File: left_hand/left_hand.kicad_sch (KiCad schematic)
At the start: 44 parts, among them J1 8P8C_Shielded, J2 Conn_01x03, J3 Conn_01x08, J4 Conn_01x08, M1 Motor_Servo, M2 Motor_Servo, M3 Motor_Servo, M4 Motor_Servo, M5 Motor_Servo, Q1 Q_NMOS_GDS, Q2 Q_NMOS_GDS, Q3 Q_NMOS_GDS, Q4 Q_NMOS_GDS, Q5 Q_NMOS_GDS, U1 MCP23017_SP, U2 PCA9615DP, U3 PCA9685PW

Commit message: Major update
Hand PCB mostly complete
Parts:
- removed C3: 0.1uF, Capacitor_THT:C_Disc_D8.0mm_W2.5mm_P5.00mm, symbol Device:C
- removed J2: Conn_01x03, Connector_PinHeader_2.54mm:PinHeader_1x03_P2.54mm_Vertical, symbol Connector_Generic:Conn_01x03
- removed J3: Conn_01x08, Connector_PinHeader_2.54mm:PinHeader_1x08_P2.54mm_Vertical, symbol Connector_Generic:Conn_01x08
- removed R1, R3, R4, R6: 120R, symbol Device:R_US
- removed R2, R5: 600R, symbol Device:R_US
- removed R7, R8: 10kR, symbol Device:R_US
- removed SO1, SO2, SO3, SO4, SO5: ~, symbol bh_symbol_library:SOLENOID
- removed U2: PCA9615DP, Package_SO:TSSOP-10_3x3mm_P0.5mm, symbol Interface:PCA9615DP
- added D6, D7: LED, LED_THT:LED_D5.0mm_Clear, symbol Device:LED
- added H1, H2, H3, H4: MountingHole, MountingHole:MountingHole_3.2mm_M3, symbol Mechanical:MountingHole
- added J5: Conn_02x02_Top_Bottom, Connector_Molex:Molex_Mini-Fit_Jr_5569-04A2_2x02_P4.20mm_Horizontal, symbol Connector_Generic:Conn_02x02_Top_Bottom
- added J6: Screw_Terminal_01x10, TerminalBlock_Phoenix:TerminalBlock_Phoenix_PT-1,5-10-5.0-H_1x10_P5.00mm_Horizontal, symbol Connector:Screw_Terminal_01x10
- added R14, R15: 330R, Resistor_THT:R_Axial_DIN0207_L6.3mm_D2.5mm_P10.16mm_Horizontal, symbol Device:R_US
- C1, C2: footprint Capacitor_THT:C_Disc_D8.0mm_W2.5mm_P5.00mm -> Capacitor_THT:C_Disc_D3.4mm_W2.1mm_P2.50mm
- J1: footprint Connector_RJ:RJ45_Amphenol_RJHSE5380 -> Connector_RJ:RJ45_Amphenol_54602-x08_Horizontal; Digikey (none) -> https://www.digikey.ca/en/products/detail/amphenol-cs-fci/5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
- M1, M2, M3, M4, M5: footprint Connector_PinHeader_2.54mm:PinHeader_1x03_P2.54mm_Horizontal -> Connector_PinHeader_2.54mm:PinHeader_1x03_P2.54mm_Vertical
- R10, R11, R12, R13, R9: footprint (none) -> Resistor_THT:R_Axial_DIN0207_L6.3mm_D2.5mm_P10.16mm_Horizontal
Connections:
- net +12V: now also J5.3 (Pin_3), J6.10 (Pin_10), J6.2 (Pin_2), J6.4 (Pin_4), J6.6 (Pin_6), J6.8 (Pin_8); no longer J1.7
- net +5V: now also J5.4 (Pin_4); no longer J1.5
- net DSCL+: now also J1.4; no longer J1.2
- net DSCL-: now also J1.3; no longer J1.1
- net DSDA+: now also J1.5; no longer J1.4
- net DSDA-: now also J1.6; no longer J1.3
- net GND: now also J1.1, J1.2, J1.7, J5.1 (Pin_1), J5.2 (Pin_2), R14.2, R15.2; no longer J1.6
- net at D5.2 (A), Q5.2 (D): now also J6.1 (Pin_1)
- net LED1: now reaches U1.26 (GPA5)
- net LED1: now also D6.2 (A)
- net LED2: now reaches U1.27 (GPA6)
- net LED2: now also D7.2 (A)
- net at D2.2 (A), Q2.2 (D): now also J6.7 (Pin_7)
- net at D3.2 (A), Q3.2 (D): now also J6.5 (Pin_5)
- net at D1.2 (A), Q1.2 (D): now also J6.9 (Pin_9)
- net at D4.2 (A), Q4.2 (D): now also J6.3 (Pin_3)
- new net: D6.1 (K), R14.1
- new net: D7.1 (K), R15.1
- no-connect marks 25 -> 23
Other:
- added sheet Differential I2C (diff_i2c.kicad_sch)
- note removed: "I2C DIFFERENTIAL TRANSCEIVER"
- moved on the sheet: D1, J1, R9, U4

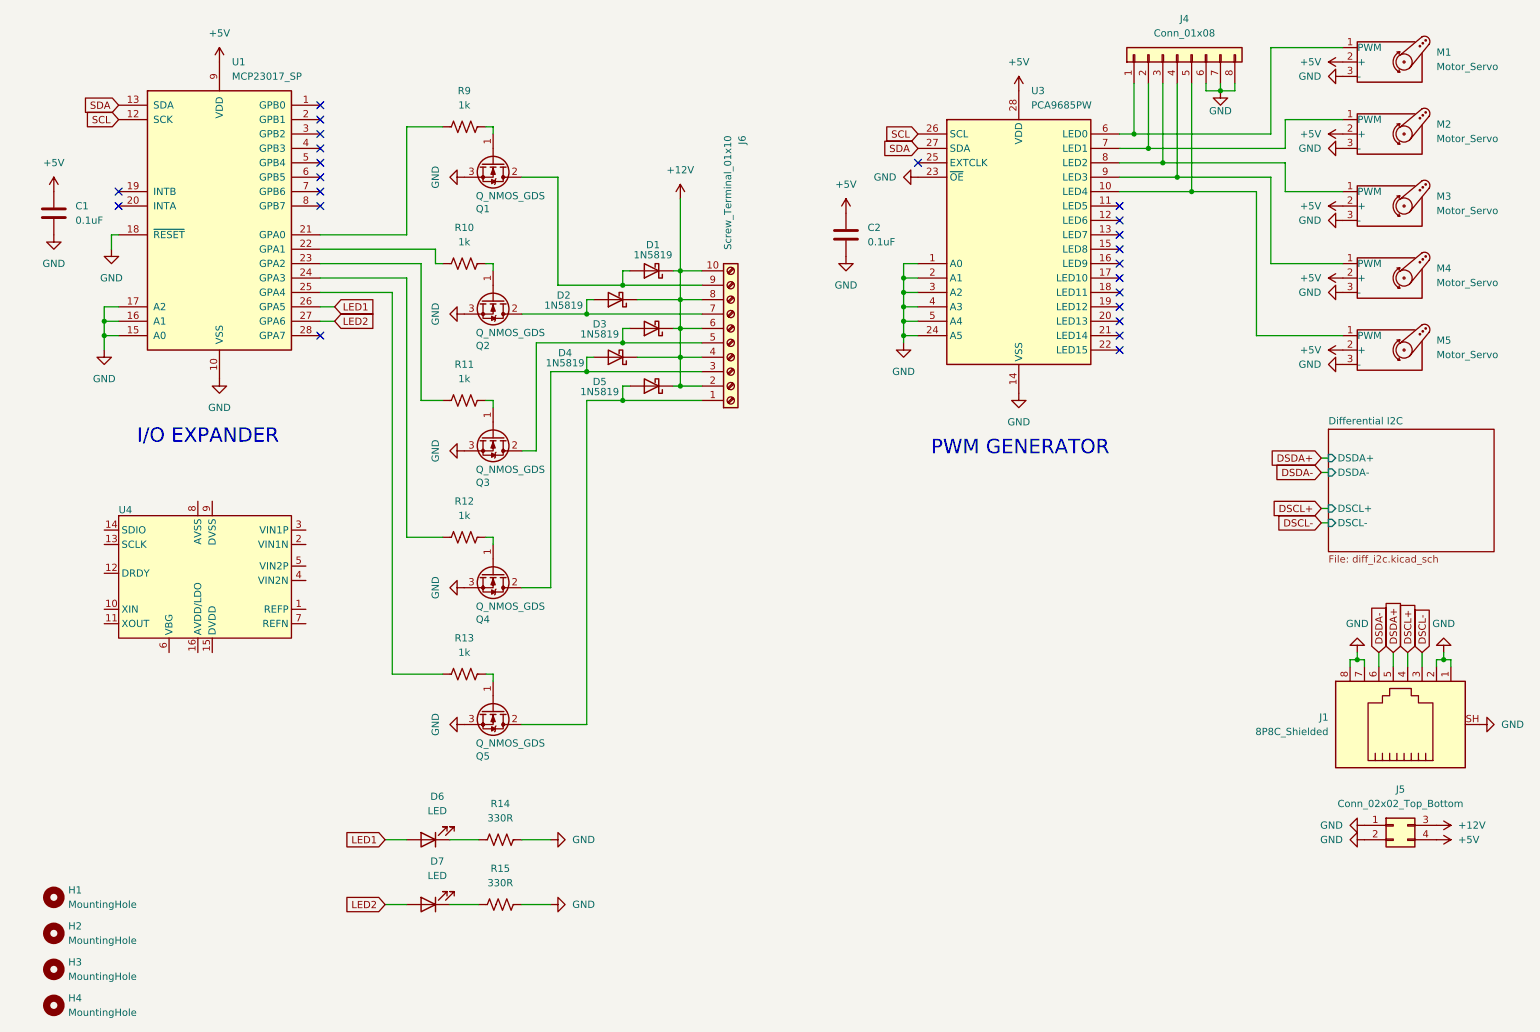
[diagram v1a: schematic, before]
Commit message: Added current and voltage sensing on control board
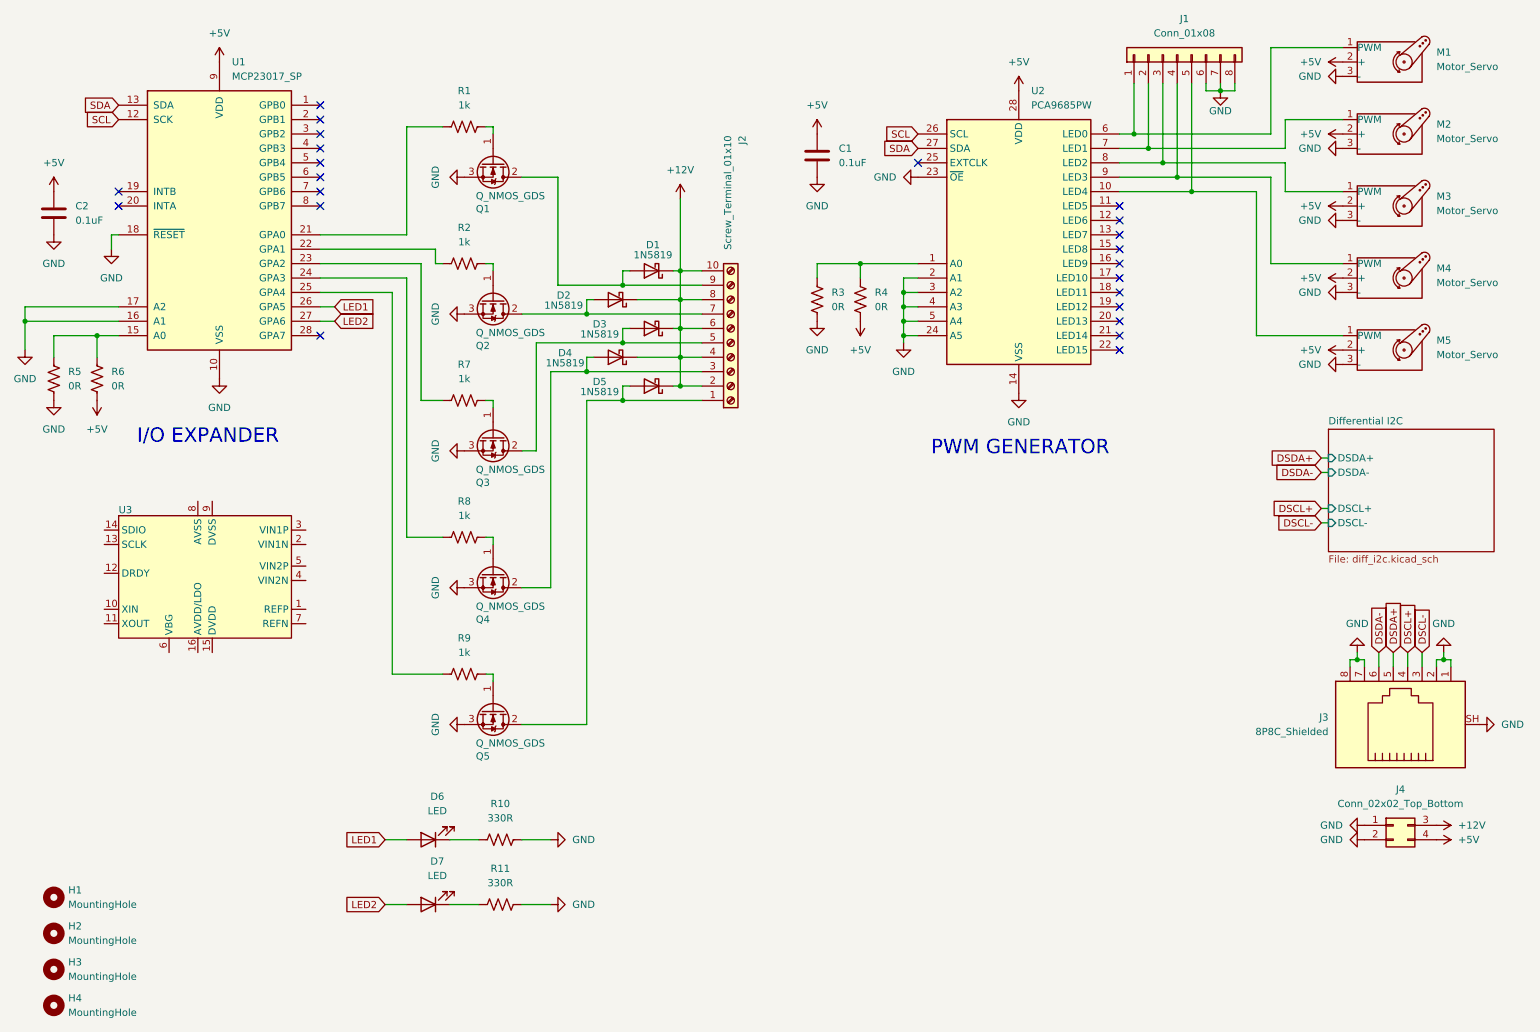
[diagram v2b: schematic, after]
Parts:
- added R3, R4, R5, R6: 0R, Resistor_THT:R_Axial_DIN0207_L6.3mm_D2.5mm_P10.16mm_Horizontal, symbol Device:R_US
- renumbered C2 to C1, C1 to C2, J4 to J1, J6 to J2, J1 to J3, J5 to J4, R9 to R1, R14 to R10, R15 to R11, R10 to R2, R11 to R7, R12 to R8, R13 to R9, U3 to U2, U4 to U3
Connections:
- net +5V: now also R4.2, R6.2
- net GND: now also R3.2, R5.2; no longer U1.15 (A0), U2.1 (A0)
- new net: R5.1, R6.1, U1.15 (A0)
- new net: R3.1, R4.1, U2.1 (A0)
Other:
- moved on the sheet: C1

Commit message: Added limit switches to hand and readme
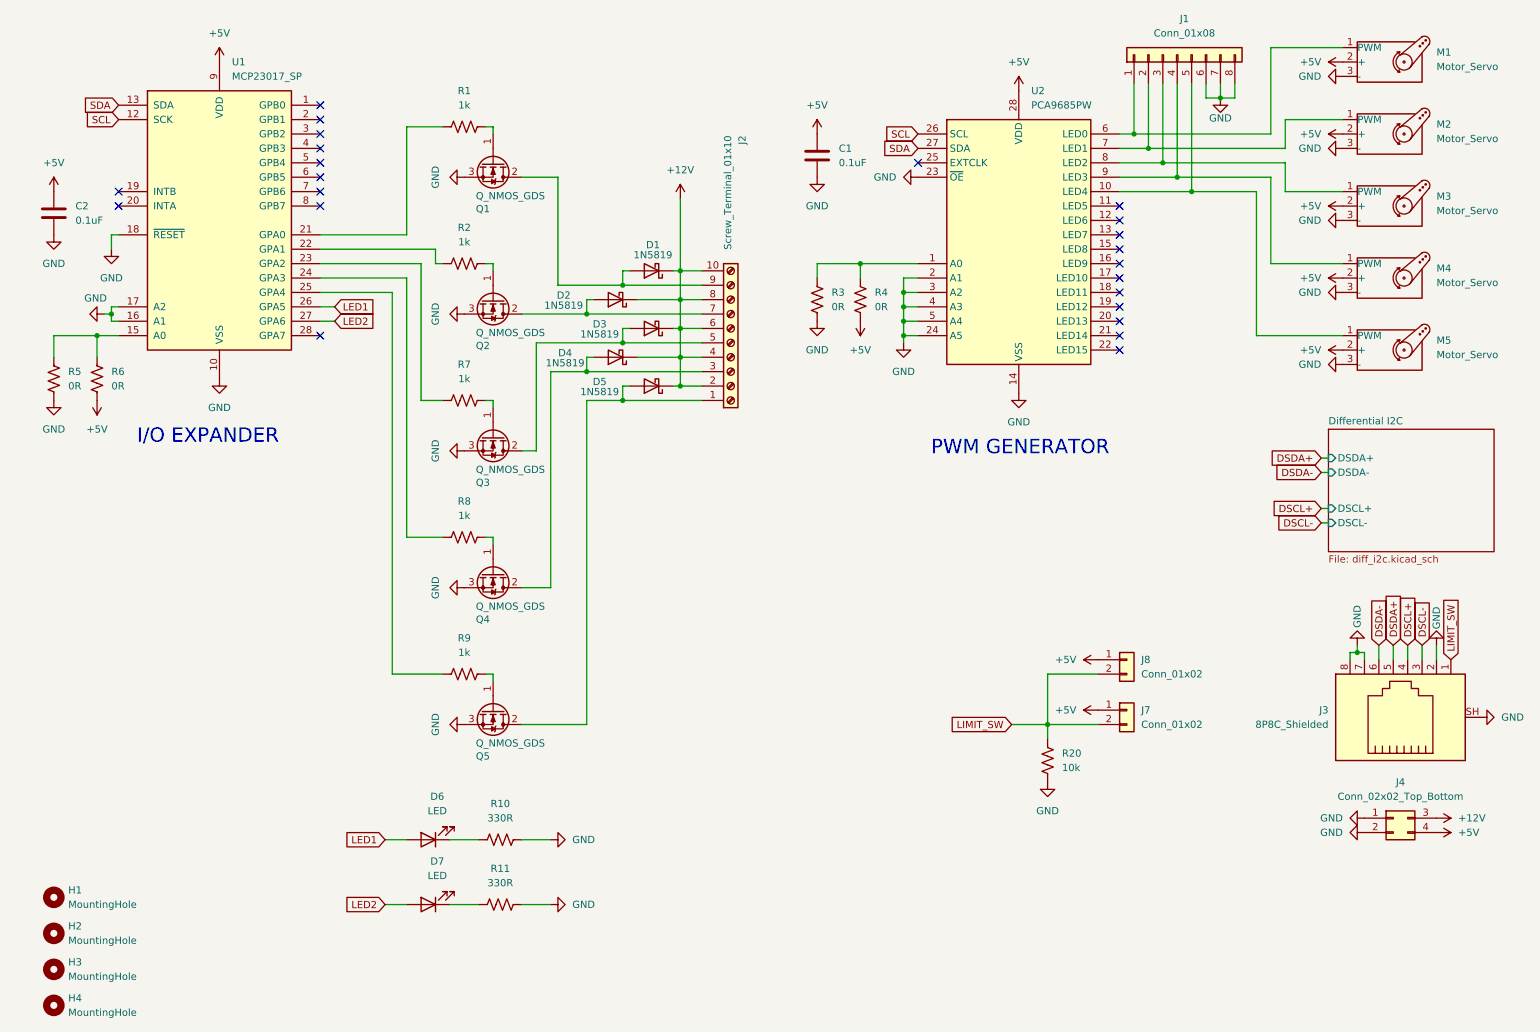
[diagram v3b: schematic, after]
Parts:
- removed U3: ~, symbol bh_symbol_library:NAU7802KGI
- added J7, J8: Conn_01x02, Connector_JST:JST_XH_S2B-XH-A_1x02_P2.50mm_Horizontal, symbol Connector_Generic:Conn_01x02
- added R20: 10k, Resistor_THT:R_Axial_DIN0207_L6.3mm_D2.5mm_P10.16mm_Horizontal, symbol Device:R_US
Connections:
- net +5V: now also J7.1 (Pin_1), J8.1 (Pin_1)
- net GND: now also R20.1; no longer J3.1
- new net LIMIT_SW: J3.1, J7.2 (Pin_2), J8.2 (Pin_2), R20.2
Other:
- moved on the sheet: J3, J4
